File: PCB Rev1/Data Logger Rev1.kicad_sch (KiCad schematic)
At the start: 13 parts, among them J1 MICRO_SD, J2 USB_B_Micro, J3 Conn_01x02_Socket, U1 ESP32-S3-MINI-1U-N8, U2 4492, U5 TPS2116DRL

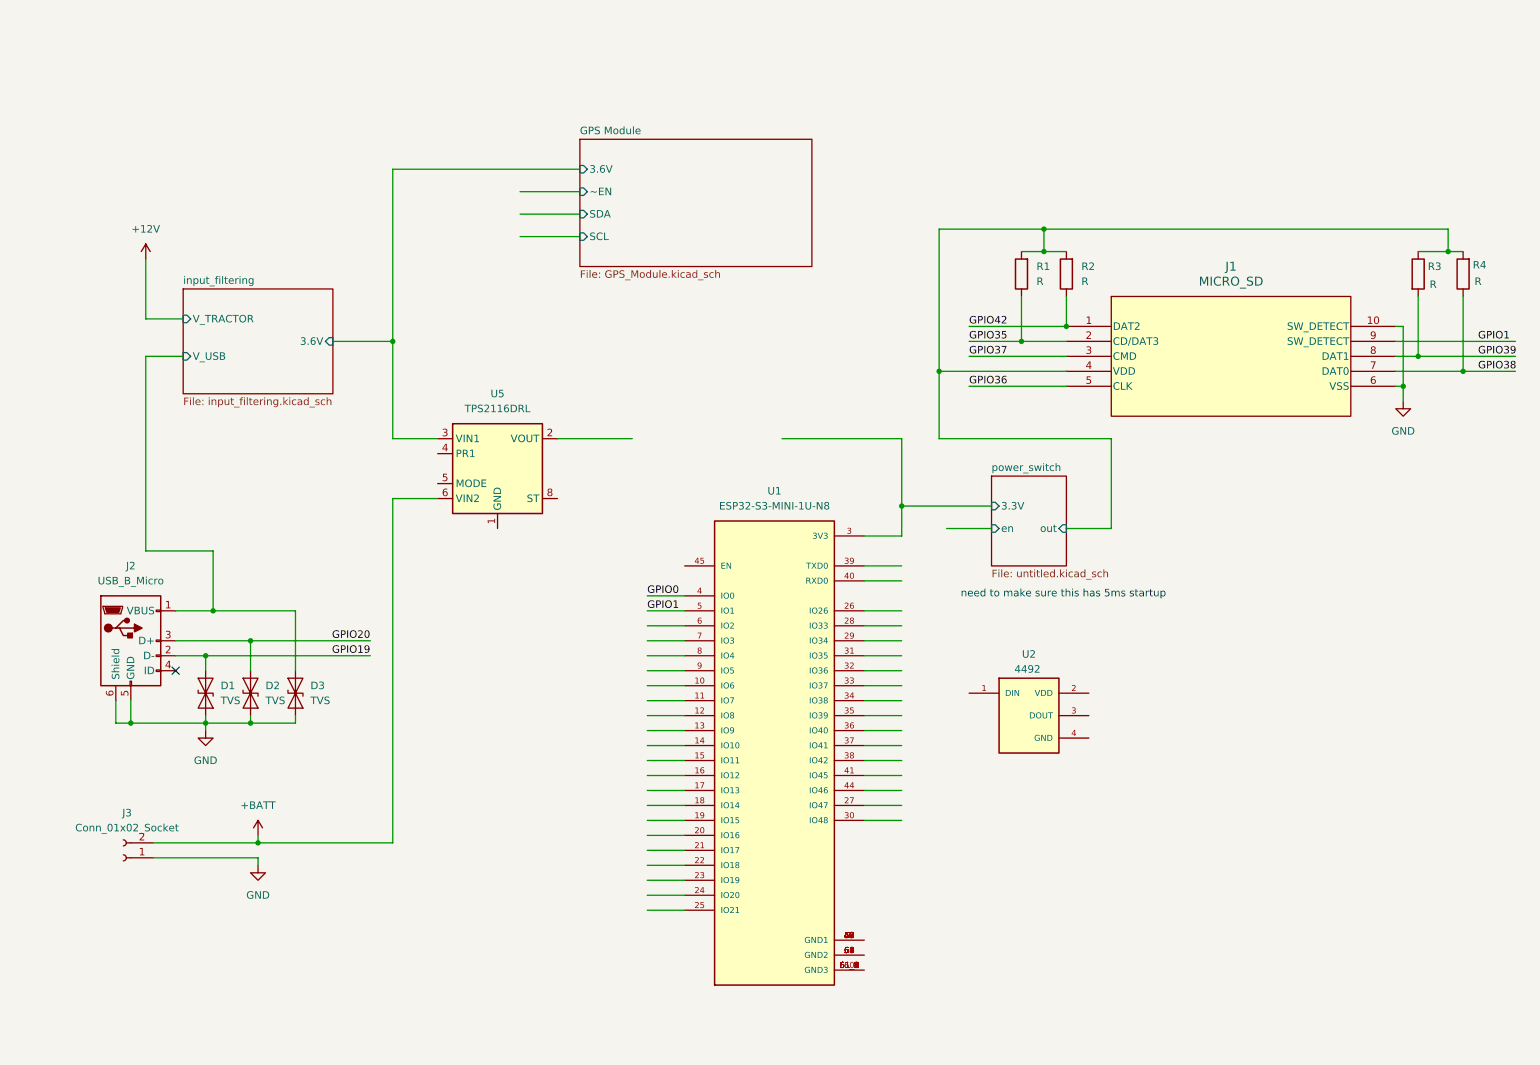
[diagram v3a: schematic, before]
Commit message: aggregated SD card and switch, updated power architecture to use 5V, added TVS diode array
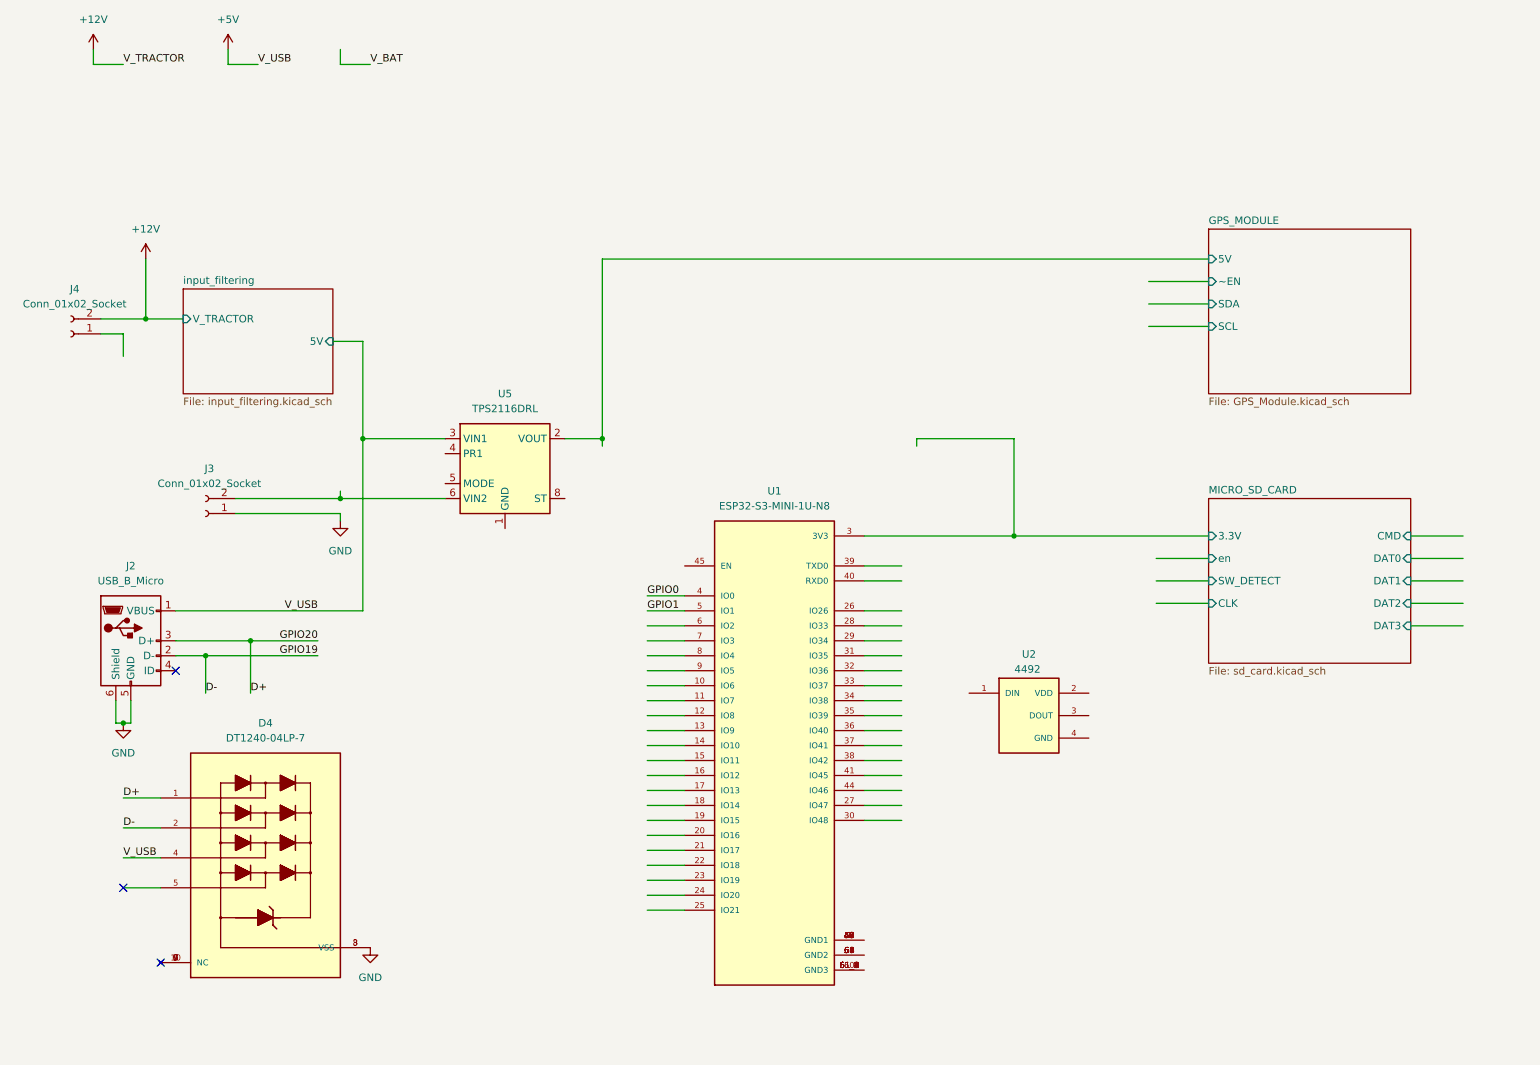
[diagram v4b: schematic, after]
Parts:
- removed D1, D2, D3: TVS, Diode_SMD:D_SMA, symbol Diode:SMAJ7.5CA
- removed J1: MICRO_SD, footprints:104031-0811_MOL, symbol sd_card_holder:1040310811
- removed R1, R2, R3, R4: R, symbol Device:R
- added D4: DT1240-04LP-7, DT1240-04LP-7:DIO_DT1240-04LP-7, symbol tvs-4chan:DT1240-04LP-7
- added J4: Conn_01x02_Socket, Connector_PinSocket_2.54mm:PinSocket_1x02_P2.54mm_Vertical, symbol Connector:Conn_01x02_Socket
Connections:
- net input_filtering/V_USB is gone; now on net +5V: J2.1 (VBUS)
- net +12V: now also J4.2 (Pin_2)
- net GND: now also D4.3 (VSS), D4.8 (VSS)
- net GPS_MODULE/5V: now reaches U5.2 (VOUT), U5.7 (VOUT)
- net +BATT: no longer names the net of J3.2 (Pin_2), U5.6 (VIN2)
- net GPIO19 renamed D-
- net D-: now also D4.2
- net GPIO20 renamed D+
- net D+: now also D4.1
- net GPS_MODULE/3.6V renamed +5V
- net +5V: now also D4.4
- net power_switch/3.3V renamed MICRO_SD_CARD/3.3V
- new net: D4.10 (NC), D4.6 (NC), D4.7 (NC), D4.9 (NC)
- no-connect marks 1 -> 3
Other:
- sheet GPS Module renamed GPS_MODULE
- removed sheet power_switch
- added sheet MICRO_SD_CARD (sd_card.kicad_sch)
- sheet GPS_MODULE ports: added 5V; removed 3.6V
- sheet input_filtering ports: added 5V; removed 3.6V, V_USB
- note removed: "need to make sure this has 5ms startup"
- moved on the sheet: J3, U5

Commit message: small changes
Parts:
- J3: value Conn_01x02_Socket -> BATTERY_PLUG (JST CONNECTOR??)
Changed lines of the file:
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@@
 			)
 		)
-		(property "Value" "Conn_01x02_Socket"
+		(property "Value" "BATTERY_PLUG (JST CONNECTOR??)"
 			(at 46.355 96.52 0)
 			(effects

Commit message: hey now, over under 5 more hours of work?
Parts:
- removed D4: DT1240-04LP-7, DT1240-04LP-7:DIO_DT1240-04LP-7, symbol tvs-4chan:DT1240-04LP-7
- removed U2: 4492, footprints:LED_4492, symbol Neopixel:4492
- removed U5: TPS2116DRL, Package_TO_SOT_SMD:SOT-583-8, symbol Power_Management:TPS2116DRL
- added D4: SP0503BAHTG, footprints:SOT143, symbol tvs:SP0503BAHTG
- added U8: SAM-M10Q, RF_GPS:ublox_SAM-M8Q, symbol RF_GPS:SAM-M8Q
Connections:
- net +5V: now also D4.4
- net D+: now also D4.3
- net D-: now also D4.2
- net GND: now also J4.1 (Pin_1), D4.1, U8.1 (GND), U8.10 (GND), U8.11 (GND), U8.15 (GND), U8.16 (GND), U8.20 (GND), U8.3 (V_BCKP), U8.4 (GND), U8.5 (GND), U8.6 (GND)
- net LOAD_SHARING_&_BAT_CHRG/V_BAT: now reaches J3.2 (Pin_2)
- net GPIO0: no longer names the net of U1.4 (IO0)
- net GPIO1: no longer names the net of U1.5 (IO1)
- net MICRO_SD_CARD/3.3V renamed +3.3V
- new net EN_SWITCH/V_OUT: U8.17 (VCC), U8.2 (VCC_IO)
- new net SCL: U8.12 (SCL)
- new net SDA: U8.9 (SDA)
- no-connect marks 3 -> 7
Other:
- sheet input_filtering renamed 12V->5V BUCK
- removed sheet GPS_MODULE
- added sheet 5V-3.7V -> 3.3V (ldo.kicad_sch)
- added sheet EN_SWITCH (AP22653Q.kicad_sch)
- added sheet LOAD_SHARING_&_BAT_CHRG (battery_management.kicad_sch)
- sheet MICRO_SD_CARD ports: added none; removed en
- note added: "1. Add TVS Diode for the tractor input 2. Make sure everything is decoupled 3. Change the USB so it looks less ugly 4. Connect up GPIOs according to code 5. Assign footprints and part numbers to passives...."
- note added: "TODO:"
- moved on the sheet: J3, U1

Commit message: added new files and switches, notes,tps
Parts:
- added D1: TVS, Diode_SMD:D_SOD-523, symbol Diode:PTVS20VZ1USK
- added JP1: Jumper_2_Open, Connector_PinHeader_2.54mm:PinHeader_1x02_P2.54mm_Vertical, symbol Jumper:Jumper_2_Open
- added R1: 10k, symbol Device:R_US
- added SW1: RESET, symbol Switch:SW_Push
- added SW2: BOOT, symbol Switch:SW_Push
- added TP1: EN, symbol Connector:TestPoint
- added TP10: CLK, symbol Connector:TestPoint
- added TP11: DAT1, symbol Connector:TestPoint
- added TP13: RXD, symbol Connector:TestPoint
- added TP14, TP15, TP16, TP17: TestPoint, symbol Connector:TestPoint
- added TP18: V_OUT_BAT_IC, symbol Connector:TestPoint
- added TP2: CMD, symbol Connector:TestPoint
- added TP3: DAT2, symbol Connector:TestPoint
- added TP4: D-, symbol Connector:TestPoint
- added TP5: TXD, symbol Connector:TestPoint
- added TP6: BOOT, symbol Connector:TestPoint
- added TP7: DAT0, symbol Connector:TestPoint
- added TP8: DAT3, symbol Connector:TestPoint
- added TP9: D+, symbol Connector:TestPoint
- renumbered D4 to D2, J4 to J1, U8 to U2
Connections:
- net +12V: now also D1.1 (K), TP14.1
- net +3.3V: now also JP1.1 (A), R1.1, TP16.1
- net +5V: now also TP15.1
- net 5V-3.7V -> 3.3V/5V/3.7V: now also TP18.1
- net CLK: now also U1.11 (IO7), TP10.1
- net CMD: now also U1.12 (IO8), TP2.1
- net D+: now also U1.24 (IO20), TP9.1
- net D-: now also U1.23 (IO19), TP4.1
- net DAT0: now also U1.13 (IO9), TP7.1
- net DAT1: now also U1.14 (IO10), TP11.1
- net DAT2: now also U1.15 (IO11), TP3.1
- net DAT3: now also U1.16 (IO12), TP8.1
- net EN: now also U1.18 (IO14)
- net GND: now also U1.1 (GND1), U1.2 (GND1), U1.42 (GND1), U1.43 (GND1), U1.46 (GND1), U1.47 (GND1), U1.48 (GND1), U1.49 (GND1), U1.50 (GND1), U1.51 (GND1), U1.52 (GND1), U1.53 (GND1), U1.54 (GND2), U1.55 (GND2), U1.56 (GND2), U1.57 (GND2), U1.58 (GND2), U1.59 (GND2), U1.60 (GND3), U1.61_1 (GND3), U1.61_2 (GND3), U1.61_3 (GND3), U1.61_4 (GND3), U1.61_5 (GND3), U1.61_6 (GND3), U1.61_7 (GND3), U1.61_8 (GND3), U1.61_9 (GND3), U1.62 (GND2), U1.63 (GND2), U1.64 (GND2), U1.65 (GND2), D1.2 (A), SW1.1, SW2.1; no longer U2.3 (V_BCKP)
- net LOAD_SHARING_&_BAT_CHRG/V_BAT: now also TP17.1
- net SW_DETECT: now also U1.17 (IO13)
- net 1SEC: now reaches U1.10 (IO6)
- net 1SEC: now also U2.7 (TIMEPULSE)
- net TXD: now reaches U1.39 (TXD0)
- net TXD: now also U2.13 (TXD), TP5.1
- net at U1.4 (IO0): now also SW2.2, TP6.1
- net RXD: now reaches U1.40 (RXD0)
- net RXD: now also U2.14 (RXD), TP13.1
- net at U1.45 (EN): now also R1.2, SW1.2, TP1.1
- net EXTINT: now reaches U1.9 (IO5)
- net EXTINT: now also U2.19 (EXTINT)
- net SCL: no longer names the net of U2.12 (SCL)
- net SDA: no longer names the net of U2.9 (SDA)
- new net: JP1.2 (B), U2.3 (V_BCKP)
- no-connect marks 7 -> 29
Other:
- added sheet ESP32-S3-MINI-1U (mcu.kicad_sch)
- note added: "1. Make sure everything is decoupled 2. Assign footprints and part numbers to passives...."
- note added: "Note: The USB Power and 12V will NOT be supplied simultaneously"
- note removed: "1. Add TVS Diode for the tractor input 2. Make sure everything is decoupled 3. Change the USB so it looks less ugly 4. Connect up GPIOs according to code 5. Assign footprints and part numbers to passives...."
- company: (none) -> California Strawberry Commission
- title: (none) -> Data Logger Rev1
- moved on the sheet: J1, U1

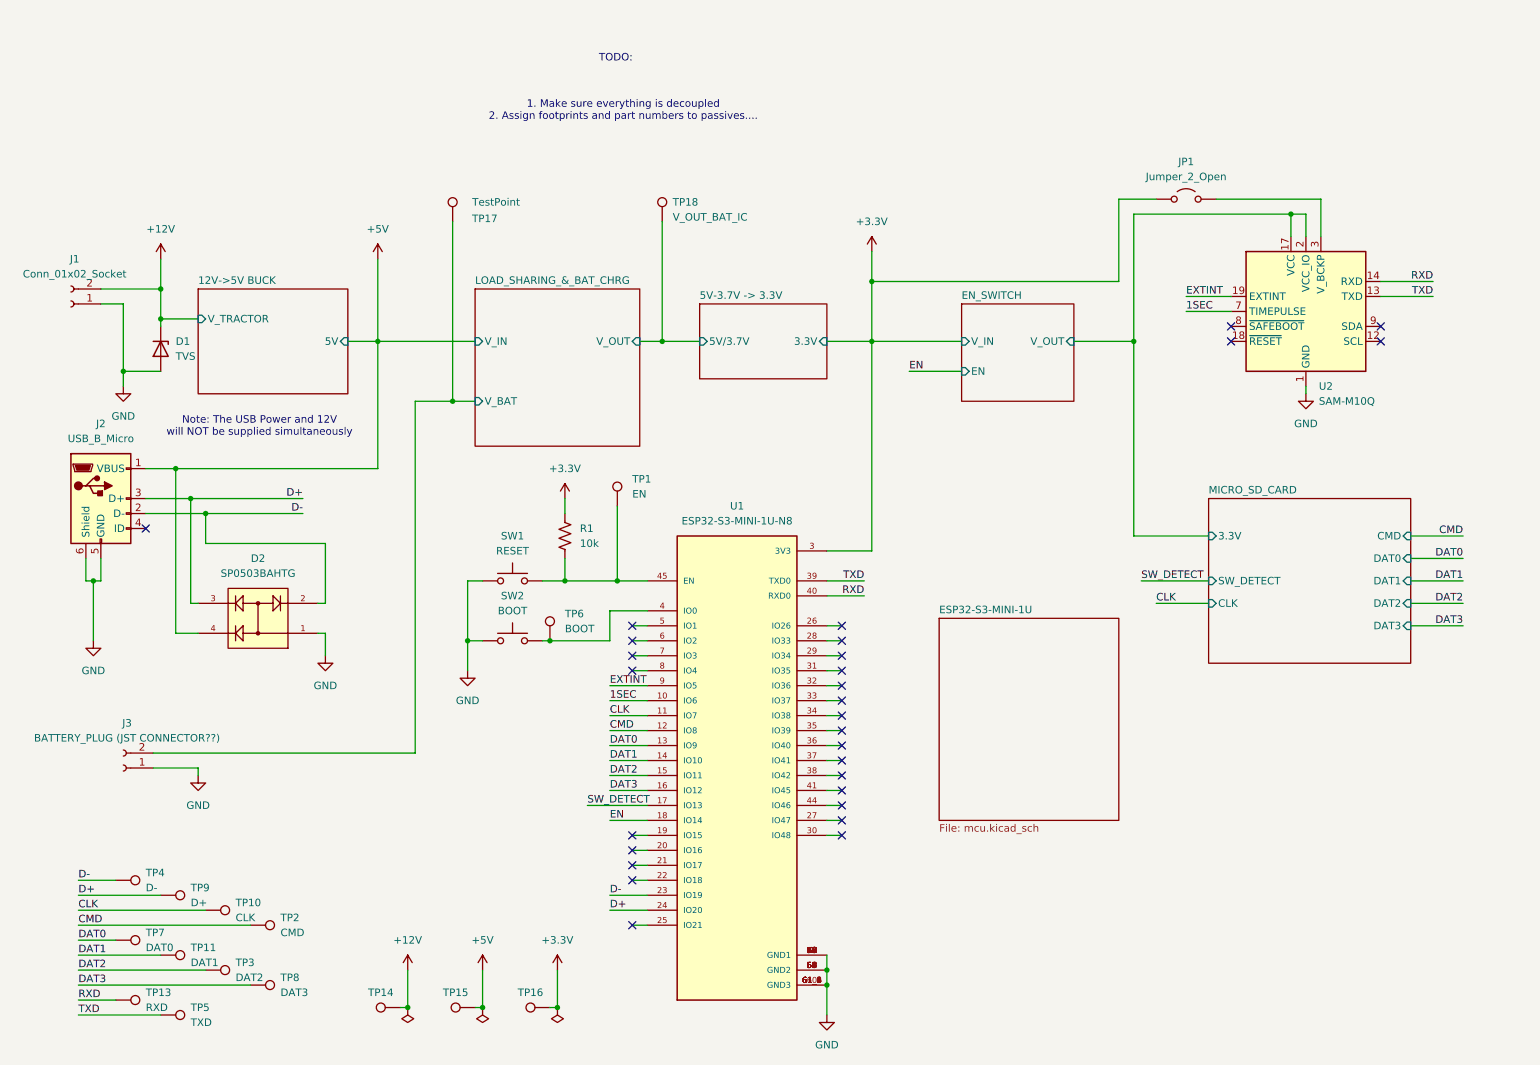
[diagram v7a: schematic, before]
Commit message: rev 2 schematic with minor changes, final send out before layout
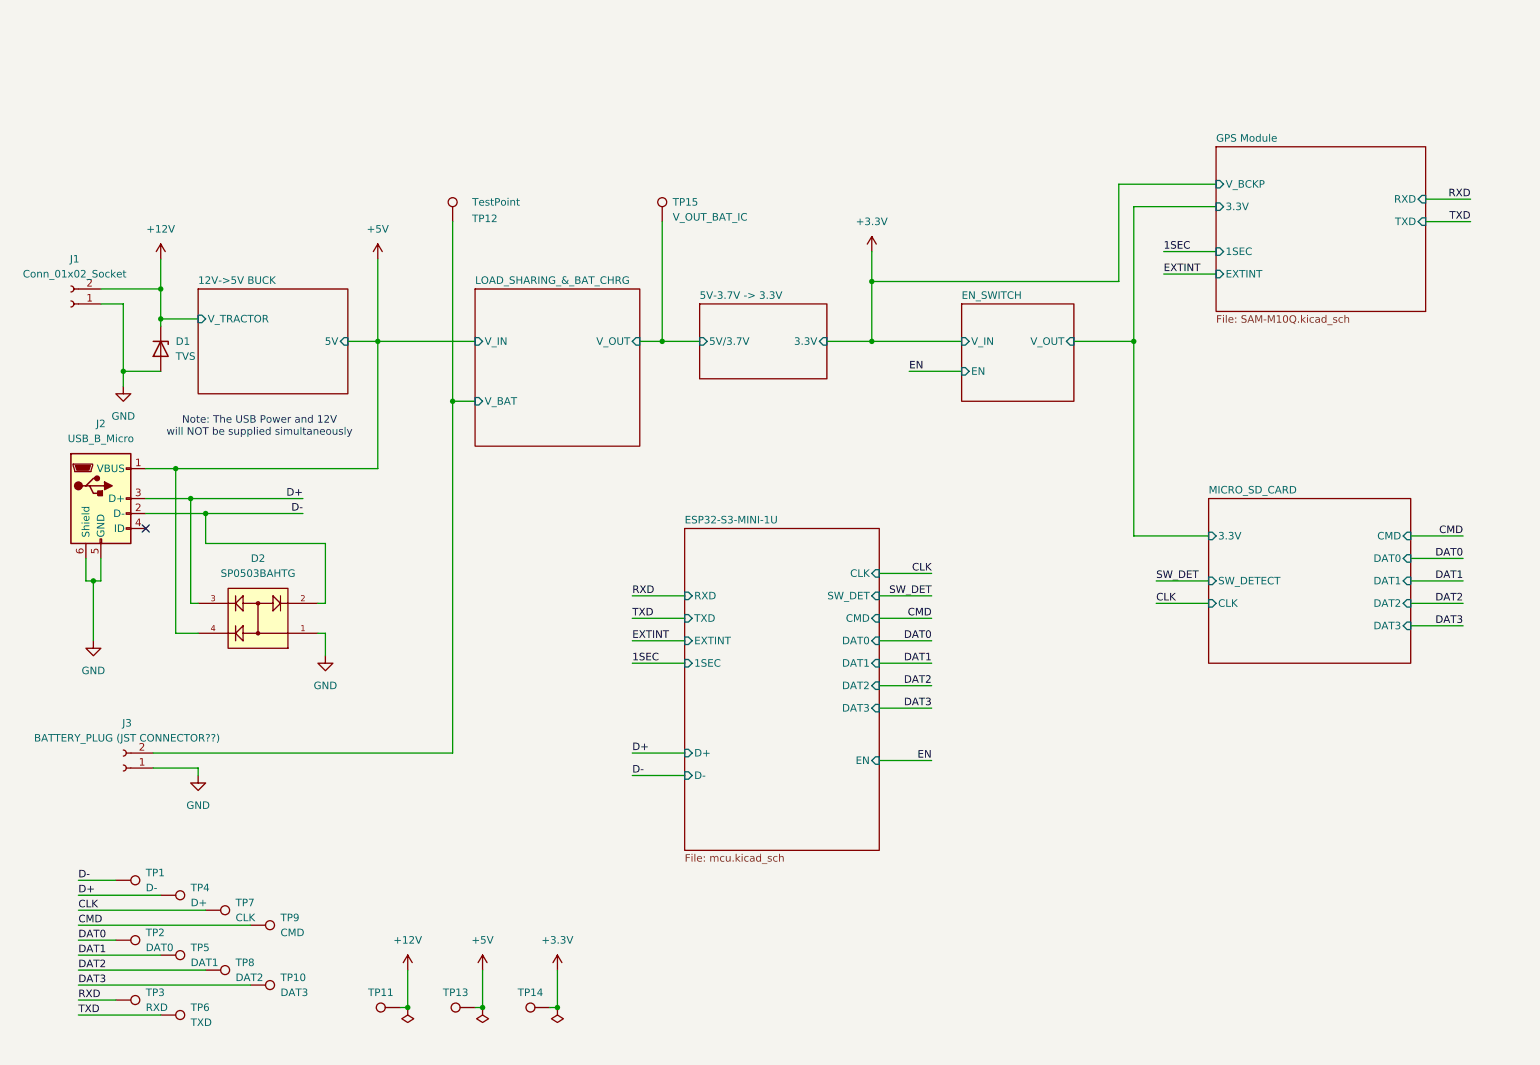
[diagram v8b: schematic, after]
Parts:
- removed JP1: Jumper_2_Open, Connector_PinHeader_2.54mm:PinHeader_1x02_P2.54mm_Vertical, symbol Jumper:Jumper_2_Open
- removed R1: 10k, symbol Device:R_US
- removed SW1: RESET, symbol Switch:SW_Push
- removed SW2: BOOT, symbol Switch:SW_Push
- removed TP1: EN, symbol Connector:TestPoint
- removed TP6: BOOT, symbol Connector:TestPoint
- removed U1: ESP32-S3-MINI-1U-N8, footprints:ESP32-S3-MINI-1U_EXP, symbol esp32-s3-..1u:ESP32-S3-MINI-1U-N8
- removed U2: SAM-M10Q, RF_GPS:ublox_SAM-M8Q, symbol RF_GPS:SAM-M8Q
- renumbered TP4 to TP1, TP8 to TP10, TP14 to TP11, TP17 to TP12, TP15 to TP13, TP16 to TP14, TP18 to TP15, TP7 to TP2, TP13 to TP3, TP9 to TP4, TP11 to TP5, TP5 to TP6, TP10 to TP7, TP3 to TP8, TP2 to TP9
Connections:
- no-connect marks 29 -> 1
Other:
- added sheet GPS Module (SAM-M10Q.kicad_sch)
- sheet ESP32-S3-MINI-1U ports: added 1SEC, CLK, CMD, D+, D-, DAT0, DAT1, DAT2, DAT3, EN, EXTINT, RXD, SW_DET, TXD; removed none
- note removed: "1. Make sure everything is decoupled 2. Assign footprints and part numbers to passives...."
- note removed: "TODO:"
